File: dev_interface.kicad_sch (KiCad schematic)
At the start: 21 parts, among them U10 ADS1014IDGS, U6 ISO164xB, U7 ADS1014IDGS, U8 TLV9301xDBV, U9 DAC53401

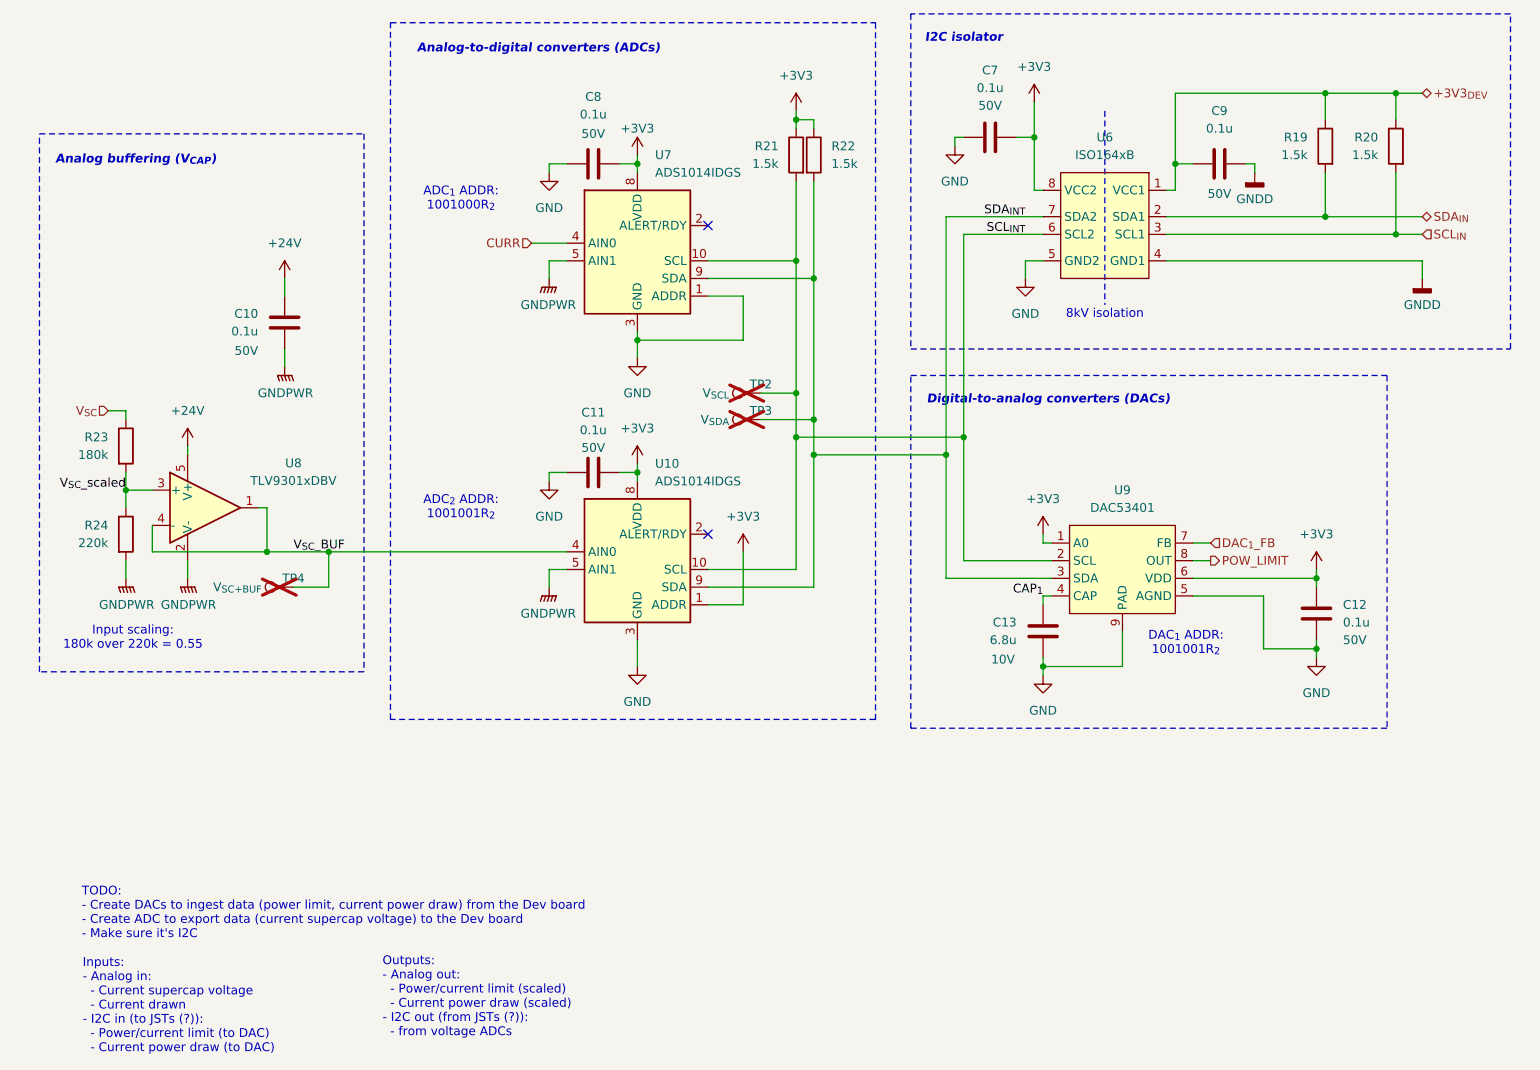
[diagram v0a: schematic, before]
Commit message: Update PCB to fix ERC breaks
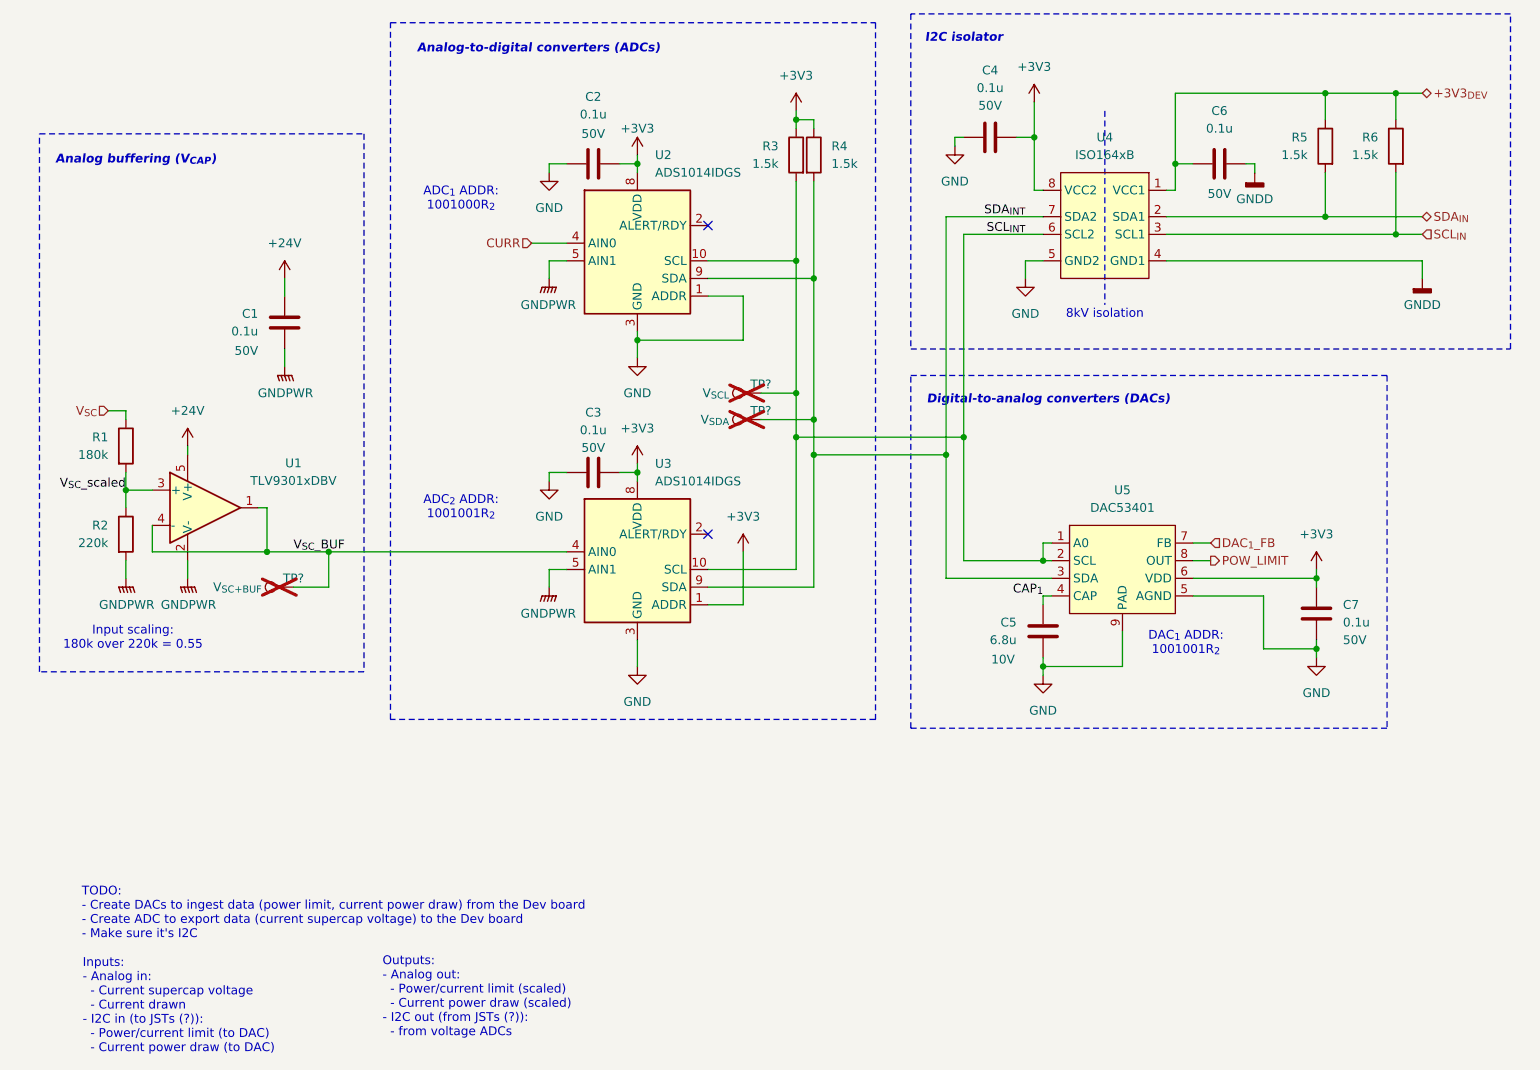
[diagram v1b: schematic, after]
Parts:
- renumbered C10 to C1, C8 to C2, C11 to C3, C7 to C4, C13 to C5, C9 to C6, C12 to C7, R23 to R1, R24 to R2, R21 to R3, R22 to R4, R19 to R5, R20 to R6, TP2 to TP?, TP3 to TP?, TP4 to TP?, U8 to U1, U7 to U2, U10 to U3, U6 to U4, U9 to U5
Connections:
- net +3V3: no longer U5.1 (A0)
- net SCL_{INT}: now also U5.1 (A0)

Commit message: Save dev interface subsheet
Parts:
- gave numbers to parts that had none: 3
- renumbered C4 to C1, C6 to C3, C1 to C4, C3 to C5, C7 to C6, C5 to C7, R5 to R1, R6 to R2, R1 to R5, R2 to R6, U4 to U1, U1 to U3, U5 to U4, U3 to U5

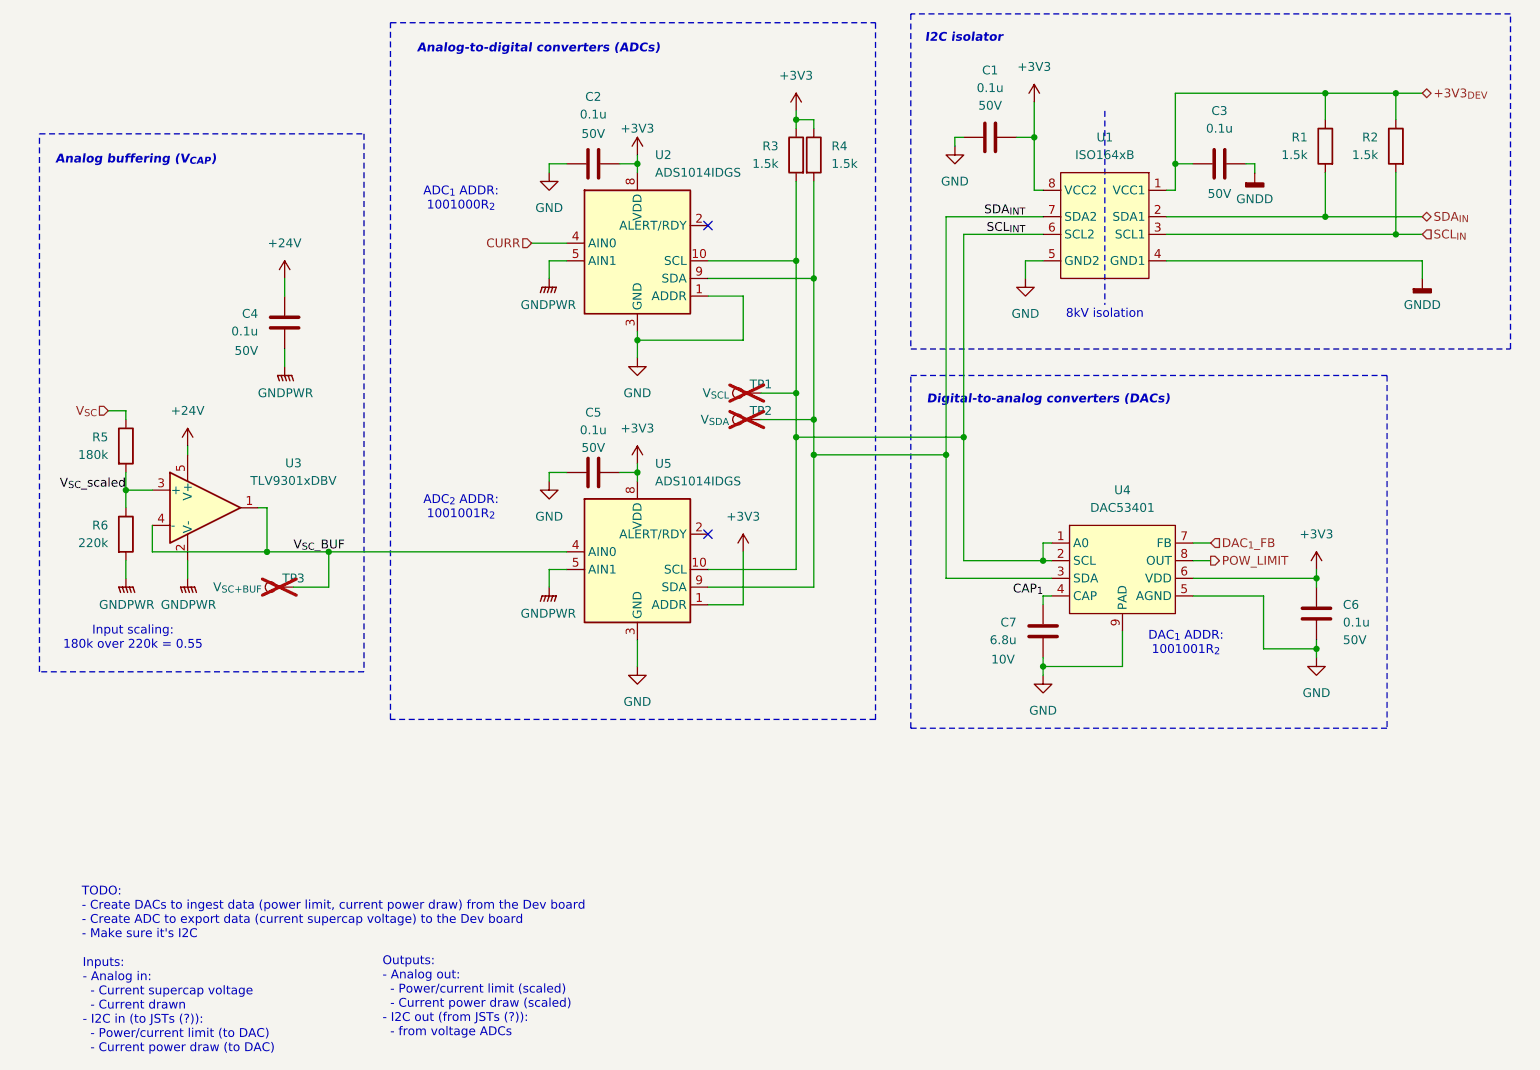
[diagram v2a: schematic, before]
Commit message: Placed footprints for boost stage 1 layout
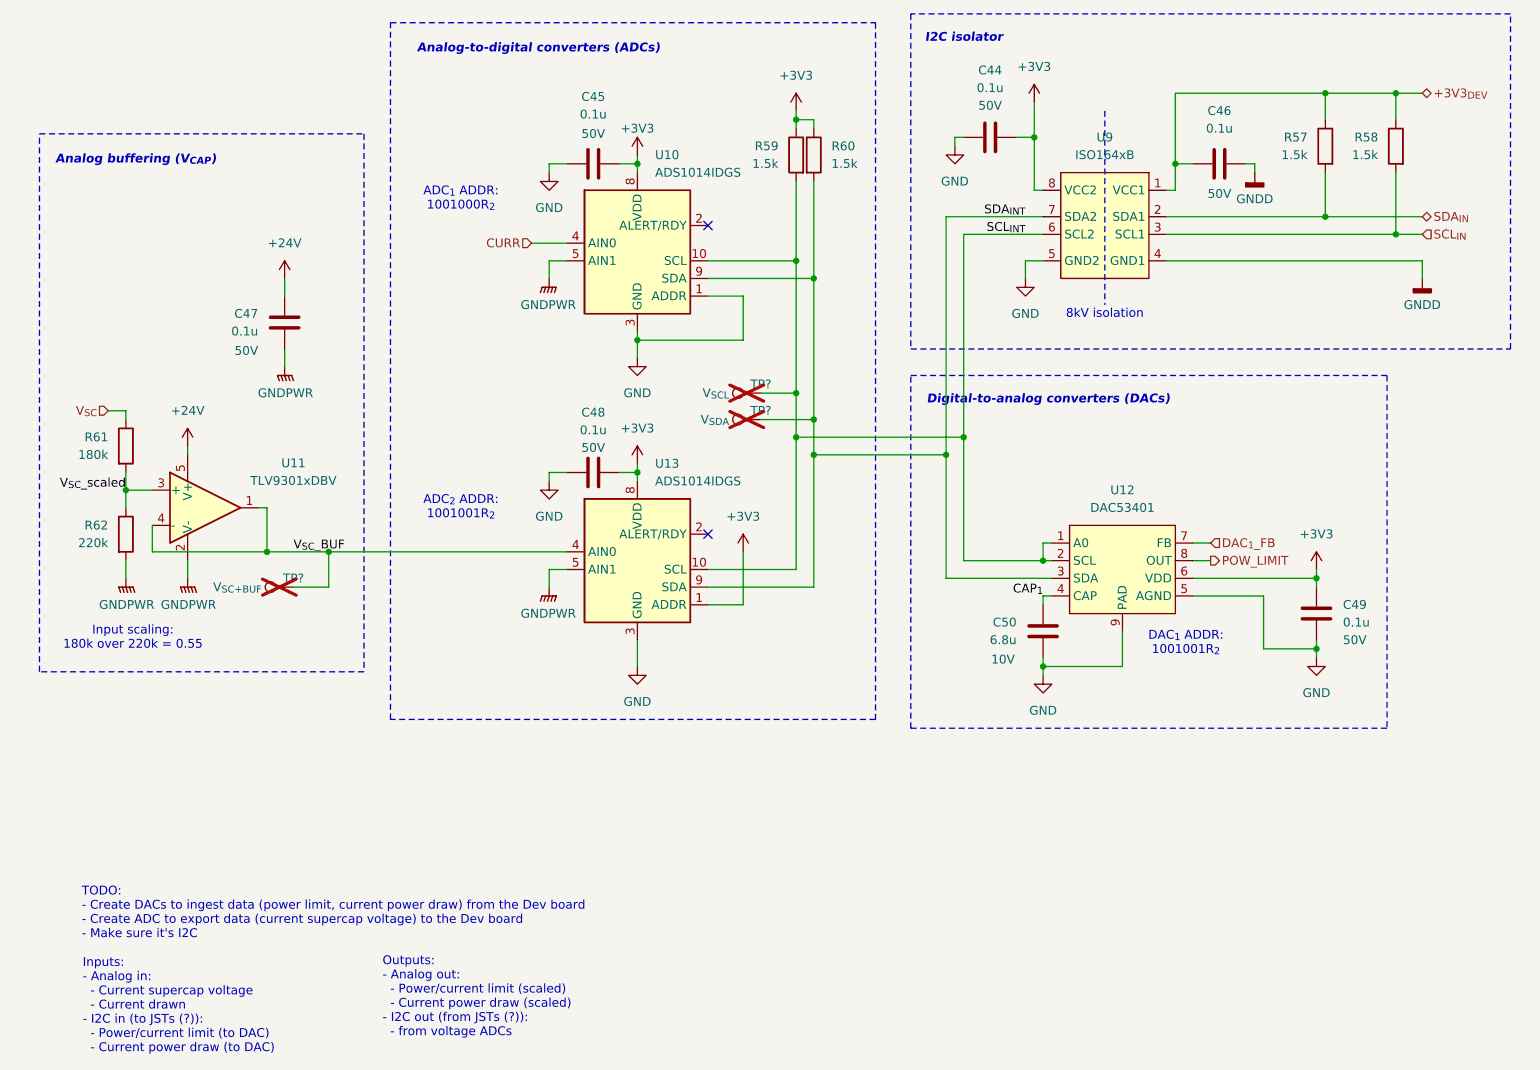
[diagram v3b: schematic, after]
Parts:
- renumbered C1 to C44, C2 to C45, C3 to C46, C4 to C47, C5 to C48, C6 to C49, C7 to C50, R1 to R57, R2 to R58, R3 to R59, R4 to R60, R5 to R61, R6 to R62, TP1 to TP?, TP2 to TP?, TP3 to TP?, U2 to U10, U3 to U11, U4 to U12, U5 to U13, U1 to U9
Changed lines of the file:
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@@
 		(on_board yes)
 		(dnp no)
-		(property "Reference" "U5"
+		(property "Reference" "U13"
 			(at 132.08 104.14 0)
 			(effects
@@
 		(dnp no)
 		(fields_autoplaced yes)
-		(property "Reference" "#PWR0101"
+		(property "Reference" "#PWR067"
 			(at 185.42 83.82 0)
 			(effects
@@
 		(dnp no)
 		(fields_autoplaced yes)
-		(property "Reference" "#PWR0110"
+		(property "Reference" "#PWR081"
 			(at 129.54 139.7 0)
 			(effects
@@
 		(dnp no)
 		(fields_autoplaced yes)
-		(property "Reference" "#PWR0122"
+		(property "Reference" "#PWR069"
 			(at 129.54 95.25 0)
 			(effects
@@
 		(on_board yes)
 		(dnp yes)
-		(property "Reference" "TP1"
+		(property "Reference" "TP?"
 			(at 147.32 92.71 90)
 			(effects
@@
 		(on_board yes)
 		(dnp no)
-		(property "Reference" "C3"
+		(property "Reference" "C46"
 			(at 213.36 53.34 90)
 			(effects
@@
 		(dnp no)
 		(fields_autoplaced yes)
-		(property "Reference" "#PWR0116"
+		(property "Reference" "#PWR064"
 			(at 218.44 68.58 0)
 			(effects
@@
 		(dnp no)
 		(fields_autoplaced yes)
-		(property "Reference" "#PWR0113"
+		(property "Reference" "#PWR060"
 			(at 152.4 57.15 0)
 			(effects
@@
 		(dnp no)
 		(fields_autoplaced yes)
-		(property "Reference" "R3"
+		(property "Reference" "R59"
 			(at 149.86 58.4199 0)
 			(effects
@@
 		(dnp no)
 		(fields_autoplaced yes)
-		(property "Reference" "#PWR0114"
+		(property "Reference" "#PWR063"
 			(at 116.84 68.58 0)
 			(effects
@@
 		(on_board yes)
 		(dnp no)
-		(property "Reference" "#PWR0115"
+		(property "Reference" "#PWR062"
 			(at 129.54 63.5 0)
 			(effects
@@
 		(dnp no)
 		(fields_autoplaced yes)
-		(property "Reference" "U4"
+		(property "Reference" "U12"
 			(at 199.39 107.95 0)
 			(effects
@@
 		(on_board yes)
 		(dnp no)
-		(property "Reference" "C7"
+		(property "Reference" "C50"
 			(at 184.15 126.9999 0)
 			(effects
@@
 		(on_board yes)
 		(dnp no)
-		(property "Reference" "C4"
+		(property "Reference" "C47"
 			(at 74.93 82.5499 0)
 			(effects
@@
 		(on_board yes)
 		(dnp no)
-		(property "Reference" "C1"
+		(property "Reference" "C44"
 			(at 180.34 47.498 90)
 			(effects
@@
 		(dnp no)
 		(fields_autoplaced yes)
-		(property "Reference" "#PWR0123"
+		(property "Reference" "#PWR072"
 			(at 129.54 107.95 0)
 			(effects
@@
 		(on_board yes)
 		(dnp no)
-		(property "Reference" "U2"
+		(property "Reference" "U10"
 			(at 132.08 59.69 0)
 			(effects
@@
 		(dnp no)
 		(fields_autoplaced yes)
-		(property "Reference" "#PWR0108"
+		(property "Reference" "#PWR071"
 			(at 64.77 105.41 0)
 			(effects
@@
 		(on_board yes)
 		(dnp no)
-		(property "Reference" "R4"
+		(property "Reference" "R60"
 			(at 157.48 58.4199 0)
 			(effects
@@
 		(dnp no)
 		(fields_autoplaced yes)
-		(property "Reference" "#PWR0107"
+		(property "Reference" "#PWR070"
 			(at 78.74 95.25 0)
 			(effects
@@
 		(dnp no)
 		(fields_autoplaced yes)
-		(property "Reference" "#PWR0121"
+		(property "Reference" "#PWR075"
 			(at 144.78 120.65 0)
 			(effects
@@
 		(dnp no)
 		(fields_autoplaced yes)
-		(property "Reference" "#PWR0104"
+		(property "Reference" "#PWR065"
 			(at 78.74 81.28 0)
 			(effects
@@
 		(on_board yes)
 		(dnp yes)
-		(property "Reference" "TP2"
+		(property "Reference" "TP?"
 			(at 147.32 96.52 90)
 			(effects
@@
 		(dnp no)
 		(fields_autoplaced yes)
-		(property "Reference" "#PWR0120"
+		(property "Reference" "#PWR077"
 			(at 227.33 123.19 0)
 			(effects
@@
 		(dnp no)
 		(fields_autoplaced yes)
-		(property "Reference" "#PWR0118"
+		(property "Reference" "#PWR082"
 			(at 187.96 140.97 0)
 			(effects
@@
 		(dnp no)
 		(fields_autoplaced yes)
-		(property "Reference" "U3"
+		(property "Reference" "U11"
 			(at 80.01 104.0698 0)
 			(effects
@@
 		(on_board yes)
 		(dnp no)
-		(property "Reference" "C5"
+		(property "Reference" "C48"
 			(at 123.19 96.774 90)
 			(effects
@@
 		(dnp no)
 		(fields_autoplaced yes)
-		(property "Reference" "#PWR0102"
+		(property "Reference" "#PWR061"
 			(at 175.26 64.77 0)
 			(effects
@@
 		(dnp no)
 		(fields_autoplaced yes)
-		(property "Reference" "R1"
+		(property "Reference" "R57"
 			(at 226.06 57.1499 0)
 			(effects
@@
 		(on_board yes)
 		(dnp no)
-		(property "Reference" "R6"
+		(property "Reference" "R62"
 			(at 53.34 113.0299 0)
 			(effects
@@
 		(on_board yes)
 		(dnp no)
-		(property "Reference" "R5"
+		(property "Reference" "R61"
 			(at 53.34 100.3299 0)
 			(effects
@@
 		(dnp no)
 		(fields_autoplaced yes)
-		(property "Reference" "#PWR0103"
+		(property "Reference" "#PWR059"
 			(at 186.69 55.88 0)
 			(effects
@@
 		(on_board yes)
 		(dnp no)
-		(property "Reference" "U1"
+		(property "Reference" "U9"
 			(at 196.85 57.15 0)
 			(effects
@@
 		(dnp no)
 		(fields_autoplaced yes)
-		(property "Reference" "#PWR0111"
+		(property "Reference" "#PWR073"
 			(at 116.84 113.03 0)
 			(effects
@@
 		(dnp no)
 		(fields_autoplaced yes)
-		(property "Reference" "#PWR0105"
+		(property "Reference" "#PWR?"
 			(at 55.88 125.73 0)
 			(effects
@@
 		)
 		(instances
+			(project "SupercapManager"
+				(path "/6197145b-e7d4-44cc-9d90-537b6501bf60/115b1a74-e36e-4ee6-8764-bf26e4e24147"
+					(reference "#PWR?")
+					(unit 1)
+				)
+			)
 			(project "DevBoardInterface 1B"
 				(path "/99fb25ed-9aca-432a-ba59-ddfa2561a3f7/c349ddf1-3671-4355-a172-174d007a1d8b"
@@
 		(on_board yes)
 		(dnp yes)
-		(property "Reference" "TP3"
+		(property "Reference" "TP?"
 			(at 80.01 120.65 90)
 			(effects
@@
 		(dnp no)
 		(fields_autoplaced yes)
-		(property "Reference" "#PWR0119"
+		(property "Reference" "#PWR080"
 			(at 227.33 138.43 0)
 			(effects
@@
 		(dnp no)
 		(fields_autoplaced yes)
-		(property "Reference" "#PWR0117"
+		(property "Reference" "#PWR068"
 			(at 242.57 83.82 0)
 			(effects
@@
 		(dnp no)
 		(fields_autoplaced yes)
-		(property "Reference" "#PWR0109"
+		(property "Reference" "#PWR066"
 			(at 116.84 82.55 0)
 			(effects
@@
 		(on_board yes)
 		(dnp no)
-		(property "Reference" "C6"
+		(property "Reference" "C49"
 			(at 231.14 124.4599 0)
 			(effects
@@
 		(on_board yes)
 		(dnp no)
-		(property "Reference" "C2"
+		(property "Reference" "C45"
 			(at 123.19 51.308 90)
 			(effects
@@
 		(dnp no)
 		(fields_autoplaced yes)
-		(property "Reference" "R2"
+		(property "Reference" "R58"
 			(at 236.22 57.1499 0)
 			(effects
@@
 		(dnp no)
 		(fields_autoplaced yes)
-		(property "Reference" "#PWR0106"
+		(property "Reference" "#PWR078"
 			(at 64.77 125.73 0)
 			(effects
@@
 		(dnp no)
 		(fields_autoplaced yes)
-		(property "Reference" "#PWR0112"
+		(property "Reference" "#PWR079"
 			(at 116.84 127 0)
 			(effects
